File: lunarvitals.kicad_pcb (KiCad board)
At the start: 2 copper layers, 48.5 x 35 mm, 39 parts, among them J1 ConductiveCord, J2 MPU6050, J3 SEN11574, J4 MAX30102, J5 USB_C_Receptacle_PowerOnly_6P, J6 Battery, Q1 FS8205, U1 NRF52840-DONGLE, U2 BMP280, U3 AP2112K-3.3, U4 TP4056, U5 MLX90614ESF-AAA-000-TU, U6 DW01A

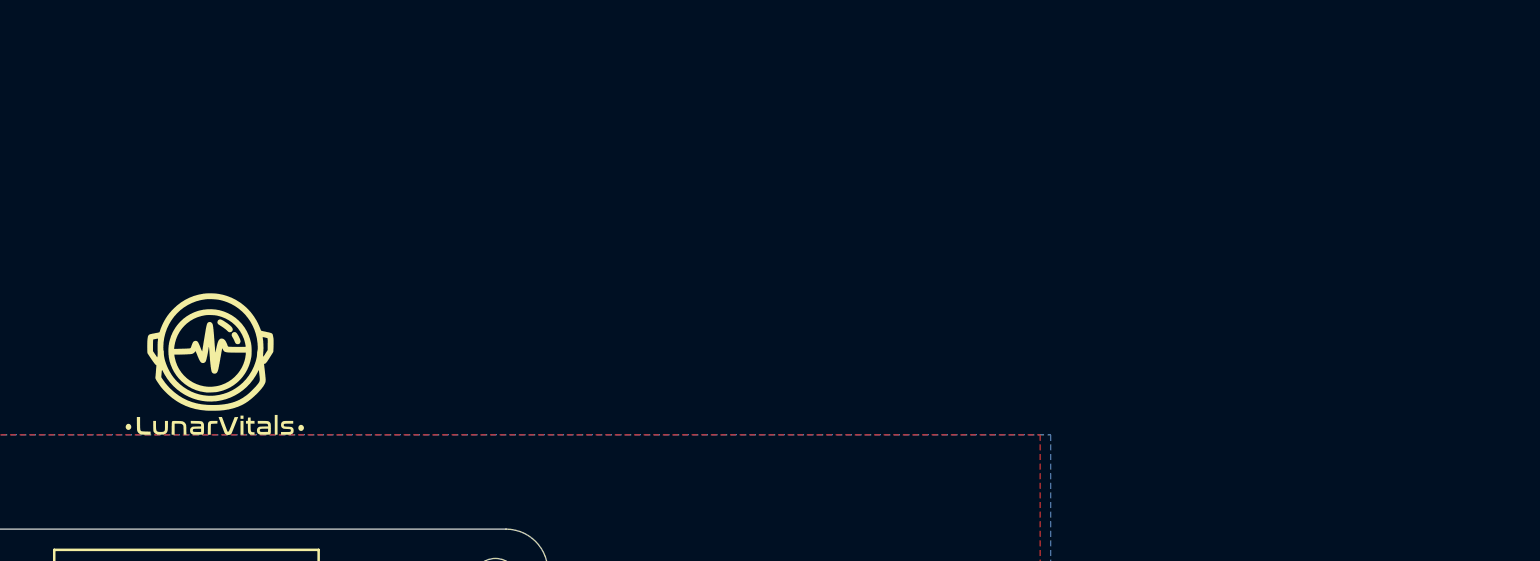
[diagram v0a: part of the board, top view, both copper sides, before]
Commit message: add 3d models to repo
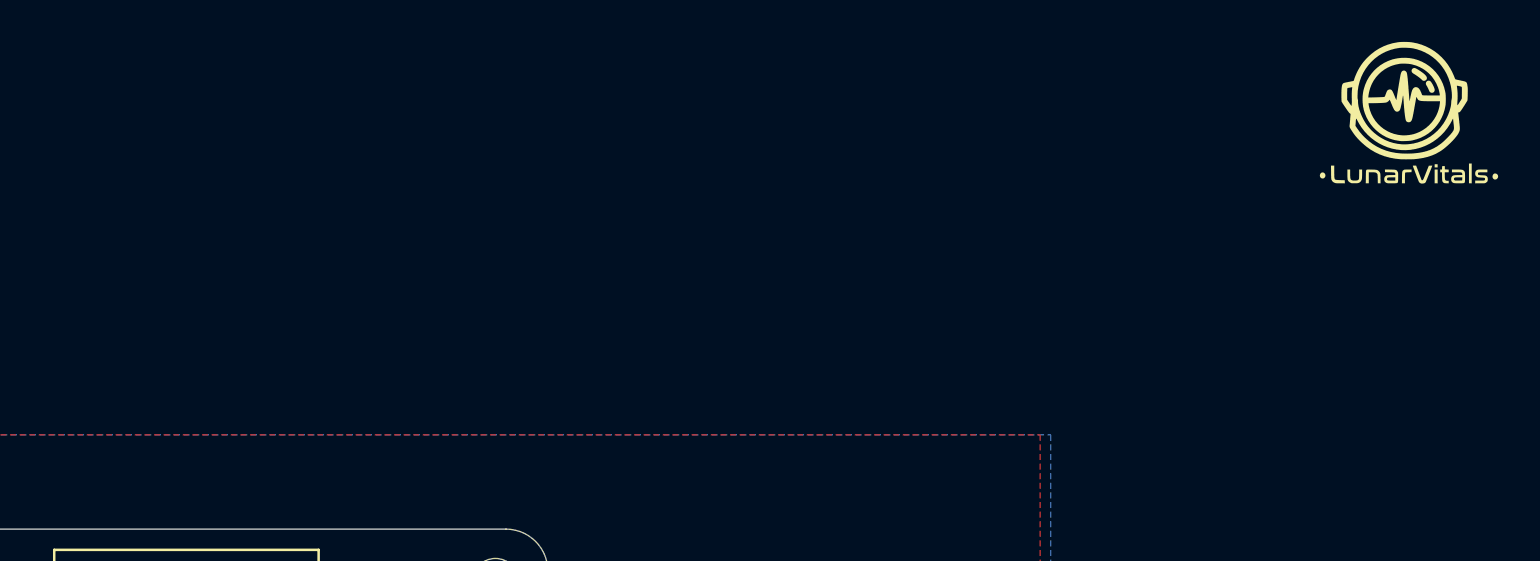
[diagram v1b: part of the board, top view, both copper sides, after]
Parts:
- moved G*** 58.2 mm to (230.5, 72.5)
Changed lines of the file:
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@@
 	(footprint "lunar_vitals_custom:lunarvitals_logo_big"
 		(layer "F.Cu")
-		(at 173.5 84.5)
+		(at 230.5 72.5)
 		(property "Reference" "G***"
 			(at 0 0 0)

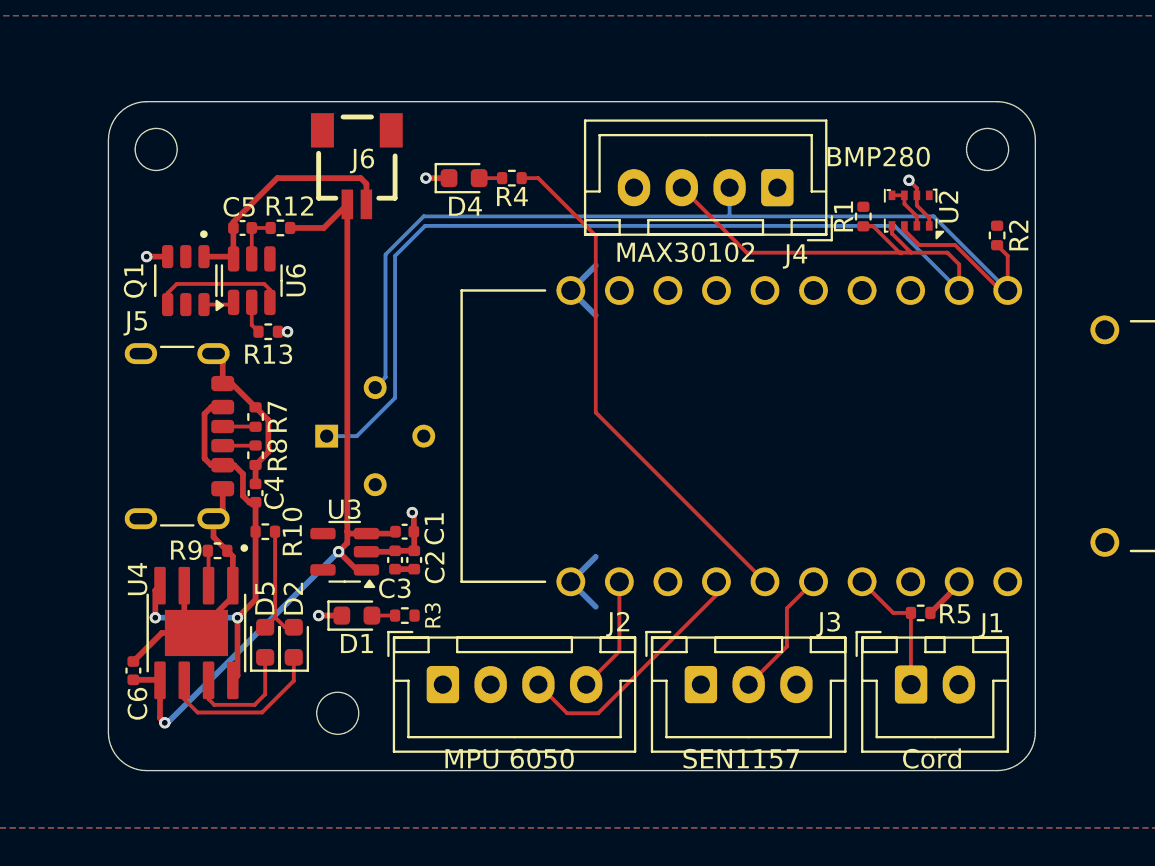
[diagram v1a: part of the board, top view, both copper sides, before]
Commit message: bmp breakout board changes (unfinished)
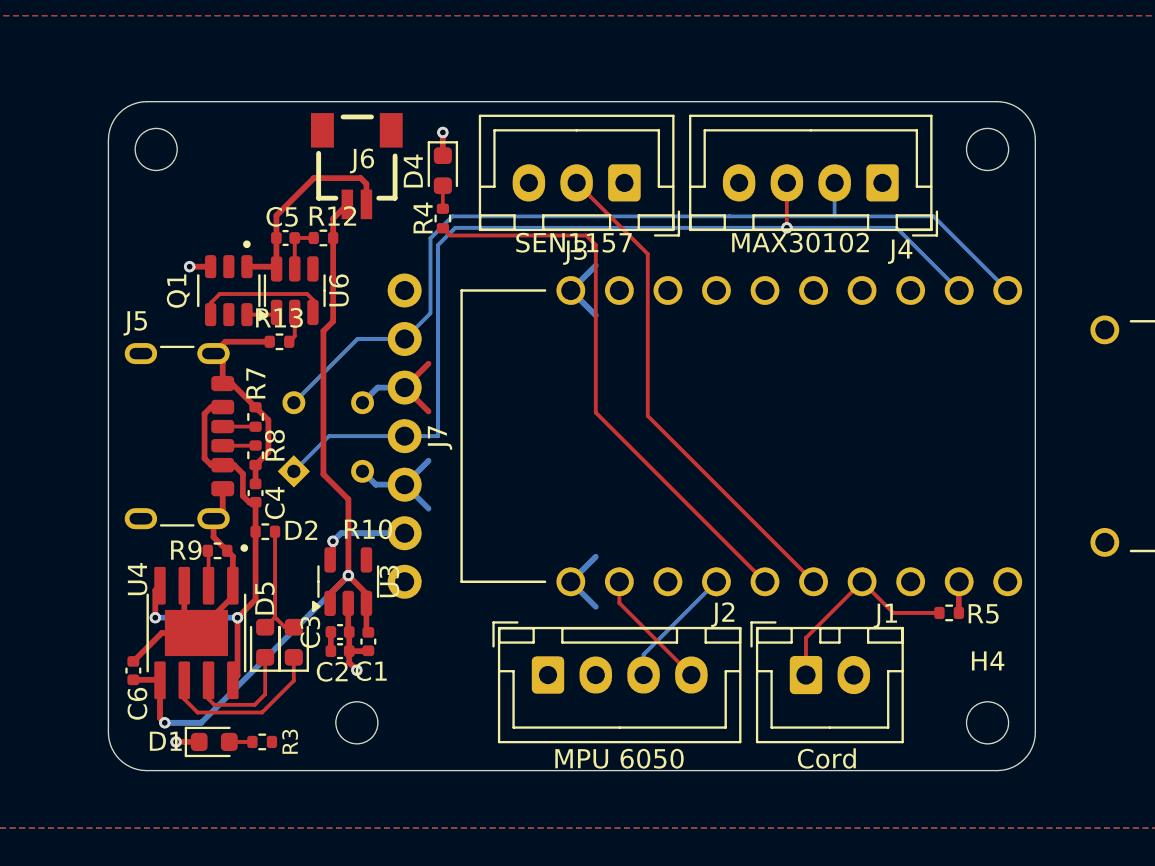
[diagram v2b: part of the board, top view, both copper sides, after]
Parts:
- removed R1, R2: 4.7k, Resistor_SMD:R_0402_1005Metric
- removed U2: BMP280, Package_LGA:Bosch_LGA-8_2x2.5mm_P0.65mm_ClockwisePinNumbering
- added H4: MountingHole, MountingHole:MountingHole_2.2mm_M2, F.Cu at (187.0, 125.0)
- added J7: Conn_01x07, lunar_vitals_custom:bmp280breakout, F.Cu at (150.2, 110.0)
- moved J3 26.6 mm to (168.0, 96.8), turned to 180 degrees
- moved D1 9.97 mm to (146.5, 126.0)
- moved R3 9.97 mm to (149.0, 126.0)
- moved C2 6.15 mm to (153.1, 121.2), turned to 0 degrees
- moved C1 6.06 mm to (154.6, 120.8), turned to -90 degrees
- moved J1 5.52 mm to (177.5, 122.5)
- moved J2 5.52 mm to (164.0, 122.5)
- moved J4 5.51 mm to (181.5, 96.8)
- moved C3 4.74 mm to (153.1, 120.2), turned to 0 degrees
- moved R4 4.18 mm to (158.5, 98.6), turned to 90 degrees
- moved U5 2.46 mm to (152.5, 110.0), turned to 45 degrees
- moved Q1 2.31 mm to (147.3, 102.4)
- moved U6 2.31 mm to (150.8, 102.4)
- moved C5 2.31 mm to (150.3, 99.6)
- moved R12 2.31 mm to (152.2, 99.6)
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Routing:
- net /AIN5: track 6.79 -> 26.0 mm
- net /I2C0_SCL: track 65.5 -> 49.8 mm, vias 0 -> 1
- net +3.3V: track 7.02 -> 13.8 mm, vias 0 -> 1
- net /I2C1_SCL: track 13.2 -> 7.15 mm
- net GND: track 43.5 -> 49.6 mm, vias 6 -> 4
- net /I2C0_SDA: track 53.2 -> 47.4 mm
- net /AIN7: track 6.98 -> 10.8 mm
- net /GPIO2: track 26.9 -> 29.7 mm
- net /B-: track 12.6 -> 11.1 mm
- net BOut+: track 42.9 -> 42.3 mm
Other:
- board text removed: "BMP280"

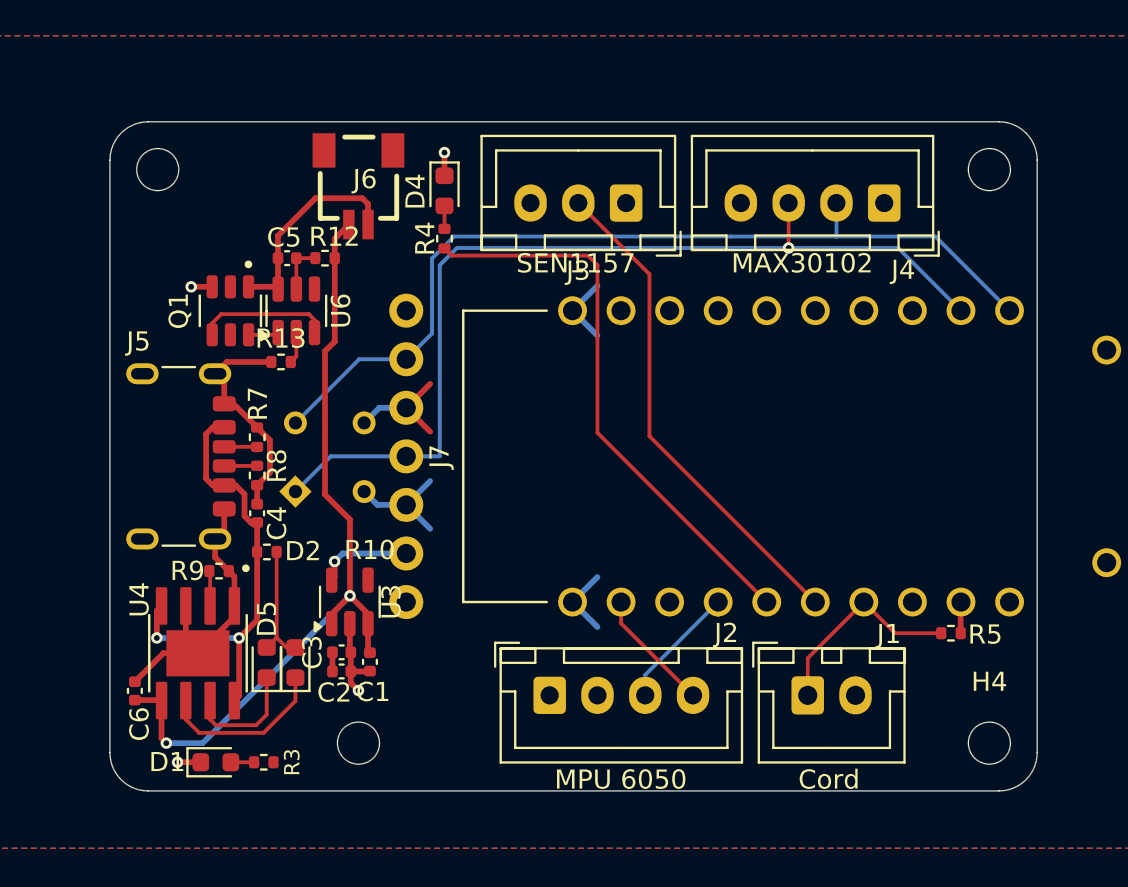
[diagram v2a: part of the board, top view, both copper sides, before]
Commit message: LED changes and BMP model
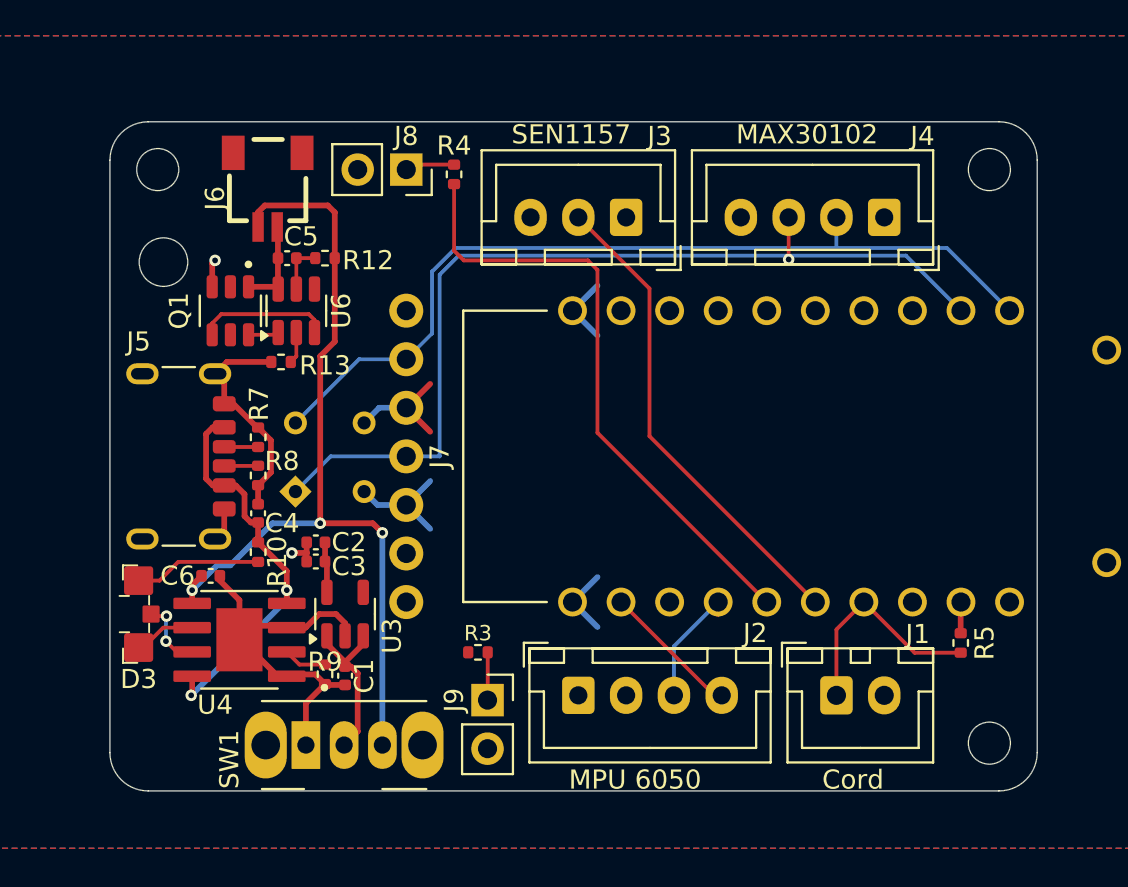
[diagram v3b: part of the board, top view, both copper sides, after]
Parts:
- removed D1: Green_LED, LED_SMD:LED_0603_1608Metric
- removed D2, D4: Red_LED, LED_SMD:LED_0603_1608Metric
- removed D5: Blue_LED, LED_SMD:LED_0603_1608Metric
- removed H3: MountingHole, MountingHole:MountingHole_2.2mm_M2
- added D3: LED_Dual_AKK, lunar_vitals_custom:KB APBA3010SURKCGKC-GX, F.Cu at (142.5, 118.2)
- added J8: Red_LED, Connector_PinSocket_2.54mm:PinSocket_1x02_P2.54mm_Vertical, F.Cu at (156.5, 95.0)
- added J9: Green_LED, Connector_PinSocket_2.54mm:PinSocket_1x02_P2.54mm_Vertical, F.Cu at (160.8, 122.8)
- added SW1: SW_SPDT, Button_Switch_THT:SW_Slide_SPDT_Angled_CK_OS102011MA1Q, F.Cu at (151.2, 125.1)
- moved R3 12.6 mm to (160.2, 120.2), turned to 0 degrees
- moved R9 7.74 mm to (152.2, 121.4), turned to -90 degrees
- moved C6 7.21 mm to (146.3, 116.2), turned to 0 degrees
- moved C2 6.88 mm to (151.8, 114.5), turned to 180 degrees
- moved C3 4.94 mm to (151.8, 115.5), turned to 180 degrees
- moved J6 4.75 mm to (149.2, 96.0)
- moved R4 3.40 mm to (159.0, 95.2)
- moved U4 2.28 mm to (147.8, 119.6), turned to 180 degrees
- moved J1 1.50 mm to (179.0, 122.5)
- moved J2 1.50 mm to (165.5, 122.5)
- moved C1 1.49 mm to (153.3, 121.5)
- moved J3 0.75 mm to (168.0, 97.5)
- moved J4 0.75 mm to (181.5, 97.5)
- moved R5 0.72 mm to (185.5, 119.8), turned to -90 degrees
- moved U3 0.68 mm to (153.3, 118.2)
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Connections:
- C1 pad 1: BOut+ -> /VSwitch
- J7 pad VIN: +3.3V -> unconnected-(J7-Pin_1-PadVIN)
- U3 pad 1: BOut+ -> /VSwitch
- U3 pad 3: BOut+ -> /VSwitch
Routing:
- net /VSwitch: track 0.00 -> 8.62 mm
- net /B-: track 11.1 -> 4.87 mm
- net Net-(D3-K2): track 8.92 -> 3.23 mm
- net BOut+: track 42.3 -> 45.9 mm, vias 2 -> 3
- net +3.3V: track 13.8 -> 10.5 mm, vias 1 -> 0
- net GND: track 49.6 -> 52.6 mm, vias 4 -> 2
- net /GPIO2: track 29.7 -> 32.4 mm
- net Net-(D3-K1): track 6.23 -> 3.78 mm, vias 0 -> 2
- net +5V: track 24.3 -> 21.9 mm
- net Net-(J8-Pin_1): track 1.20 -> 2.61 mm
- net /I2C0_SDA: track 47.4 -> 46.4 mm
- net Net-(U4-PROG): track 1.84 -> 2.83 mm
- net Net-(J9-Pin_1): track 1.53 -> 2.50 mm
- net /I2C1_SDA: track 6.44 -> 7.29 mm
- net /AIN7: track 10.8 -> 11.6 mm
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
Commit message: final changes
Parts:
- removed J8: Red_LED, Connector_PinSocket_2.54mm:PinSocket_1x02_P2.54mm_Vertical
- removed J9: Green_LED, Connector_PinSocket_2.54mm:PinSocket_1x02_P2.54mm_Vertical
- added D1: Green_LED, LED_THT:LED_D3.0mm, F.Cu at (160.2, 125.5)
- added D2: Red_LED, LED_THT:LED_D3.0mm, F.Cu at (154.7, 95.0)
- added JP1: Jumper_2_Small_Open, TestPoint:TestPoint_2Pads_Pitch2.54mm_Drill0.8mm, F.Cu at (188.2, 121.0)
- moved R5 1.76 mm to (183.8, 119.2), turned to 180 degrees
- moved R3 1.17 mm to (159.7, 121.3)
- moved SW1 1.10 mm to (150.2, 125.1)
- moved C1 0.35 mm to (152.9, 121.5)
- moved R4 0.26 mm to (159.0, 95.5)
- moved R9 0.25 mm to (152.0, 121.4)
- moved U3 0.10 mm to (153.2, 118.2)
- moved J2 0.10 mm to (165.6, 122.5)
- moved J4 0.10 mm to (181.4, 97.5)
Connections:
- C1 pad 1: /VSwitch -> BOut+
- SW1 pad 2: /VSwitch -> Net-(SW1-B)
- U1 pad VBUS: unconnected-(U1-PadVBUS) -> Net-(JP1-A)
- U3 pad 1: /VSwitch -> BOut+
- U3 pad 3: /VSwitch -> Net-(SW1-B)
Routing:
- net +5V: track 21.9 -> 64.9 mm, vias 2 -> 3
- net /VSwitch: track 8.62 -> 0.00 mm
- net Net-(SW1-B): track 0.00 -> 7.37 mm, vias 0 -> 1
- net BOut+: track 45.9 -> 50.9 mm, vias 3 -> 4
- net GND: track 52.6 -> 48.6 mm, vias 2 -> 3
- net Net-(JP1-A): track 0.00 -> 3.46 mm
- net /AIN7: track 11.6 -> 9.01 mm
- net Net-(D2-A): track 2.61 -> 1.73 mm
- net Net-(D1-A): track 2.50 -> 1.68 mm
- net +3.3V: track 10.5 -> 11.1 mm
- net /GPIO2: track 32.4 -> 31.9 mm
- net /I2C0_SCL: track 49.0 -> 48.5 mm

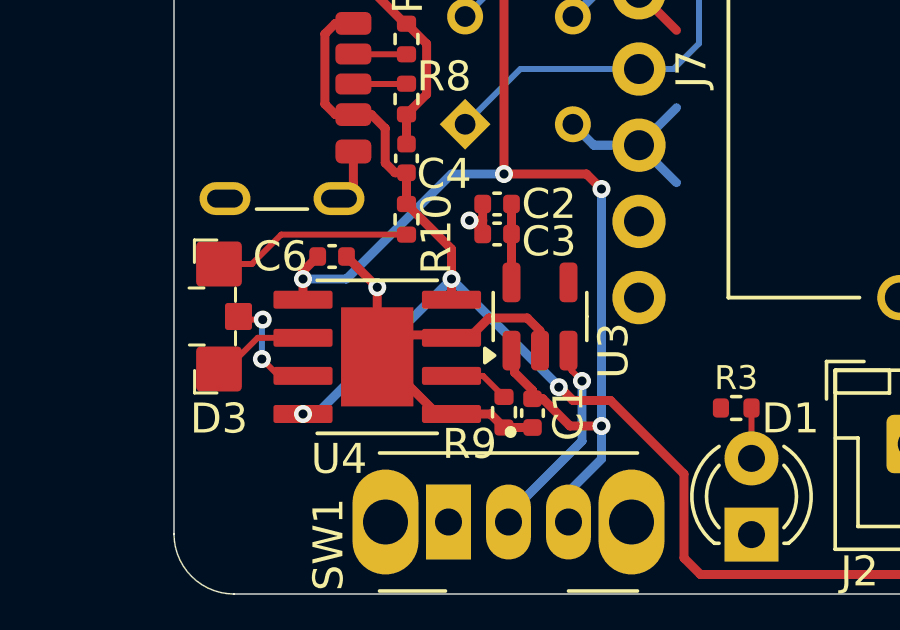
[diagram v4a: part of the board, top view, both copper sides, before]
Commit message: remove via in pad
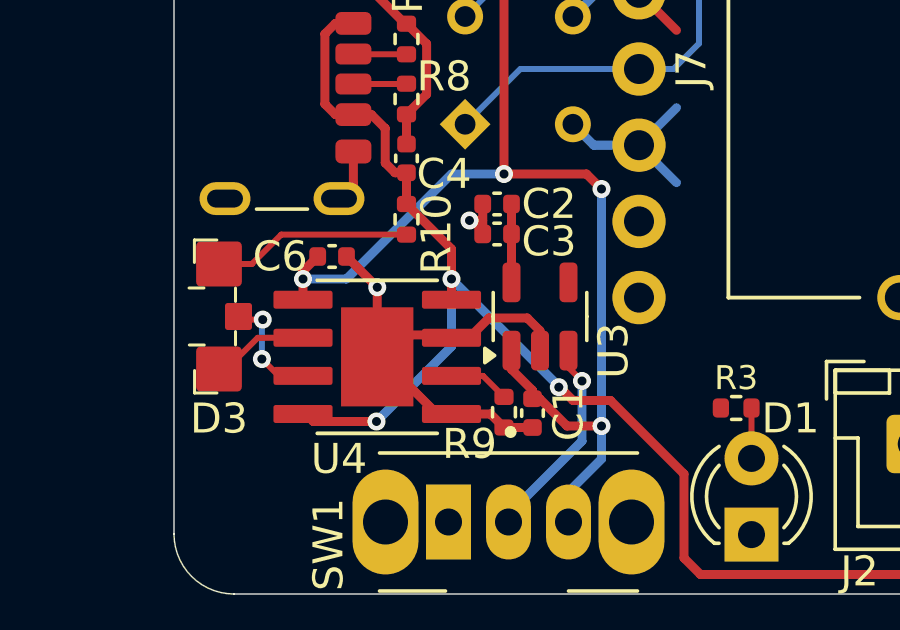
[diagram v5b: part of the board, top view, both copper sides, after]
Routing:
- net +5V: track 64.9 -> 66.4 mm
